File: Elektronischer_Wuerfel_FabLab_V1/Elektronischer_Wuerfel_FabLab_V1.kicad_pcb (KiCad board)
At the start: 2 copper layers, 20.9 x 20.9 mm, 21 parts, among them J1 Conn_01x02_Socket, J2 Conn_01x01_Socket, J3 Conn_01x06_Socket, U1 ATtiny85-20S

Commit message: some minor changes, repair of not connected A
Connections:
- U1 pad 6: unconnected-(U1-PB1-Pad6) -> /A
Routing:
- net /A: track 31.0 -> 35.4 mm, vias 0 -> 1
- net GND: track 4.86 -> 6.45 mm
- net VCC: track 10.5 -> 11.2 mm
- net /C: track 29.3 -> 29.9 mm
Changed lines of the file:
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@@
 	(net 14 "Net-(D6-A)")
 	(net 15 "Net-(D7-A)")
-	(net 16 "unconnected-(U1-PB1-Pad6)")
 	(footprint "Connector_PinHeader_2.00mm:PinHeader_1x02_P2.00mm_Vertical"
 		(layer "F.Cu")
@@
 			(size 1.7 0.65)
 			(layers "B.Cu" "B.Paste" "B.Mask")
-			(net 16 "unconnected-(U1-PB1-Pad6)")
+			(net 7 "/A")
 			(pinfunction "PB1")
 			(pintype "bidirectional")
@@
 	)
 	(segment
-		(start 176.036 73.1376)
-		(end 175.26 73.914)
+		(start 175.6075 73.5)
+		(end 176.036 73.0715)
 		(width 0.15)
 		(layer "F.Cu")
@@
 	)
 	(segment
-		(start 176.036 73.0715)
-		(end 176.036 73.1376)
+		(start 174.5 73.5)
+		(end 175.6075 73.5)
 		(width 0.15)
 		(layer "F.Cu")
@@
 	)
 	(via
-		(at 175.26 73.914)
+		(at 174.5 73.5)
 		(size 0.5)
 		(drill 0.4)
@@
 	)
 	(via
-		(at 175.26 75.184)
+		(at 175.26 75.5)
 		(size 0.5)
 		(drill 0.4)
@@
 	)
 	(segment
-		(start 175.26 73.914)
-		(end 175.26 75.184)
+		(start 174.5 73.5)
+		(end 175.26 74.26)
 		(width 0.15)
 		(layer "B.Cu")
@@
 	)
 	(segment
-		(start 172.211 70.4424)
-		(end 172.464 70.6947)
+		(start 175.26 74.26)
+		(end 175.26 75.5)
 		(width 0.15)
-		(layer "F.Cu")
-		(net 2)
+		(layer "B.Cu")
+		(net 1)
 	)
 	(segment
@@
 	)
 	(segment
-		(start 175.254 68.5073)
-		(end 174.993 68.7681)
+		(start 165.4092 71.2979)
+		(end 164.513 71.2979)
 		(width 0.15)
 		(layer "F.Cu")
@@
 	)
 	(segment
-		(start 172.464 71.0248)
-		(end 172.4635 71.0253)
+		(start 173.5 71)
+		(end 172.4888 71)
 		(width 0.15)
 		(layer "F.Cu")
@@
 	)
 	(segment
-		(start 177.333 73.7876)
-		(end 178.458 73.7876)
+		(start 172.464 71.0248)
+		(end 172.4635 71.0253)
 		(width 0.15)
 		(layer "F.Cu")
@@
 	)
 	(segment
-		(start 163.6 71.3887)
-		(end 164.422 71.3887)
+		(start 177.333 74)
+		(end 178.2455 74)
 		(width 0.15)
 		(layer "F.Cu")
@@
 	)
 	(segment
-		(start 175.76 68.5073)
-		(end 175.254 68.5073)
+		(start 178.2455 74)
+		(end 178.482 73.7635)
 		(width 0.15)
 		(layer "F.Cu")
@@
 	)
 	(segment
-		(start 178.458 73.7876)
-		(end 178.482 73.7635)
+		(start 178.23 66.548)
+		(end 178.412 66.548)
 		(width 0.15)
 		(layer "F.Cu")
@@
 	)
 	(segment
-		(start 164.422 71.3887)
-		(end 164.513 71.2979)
+		(start 172.4635 71.0253)
+		(end 172.4635 71.3549)
 		(width 0.15)
 		(layer "F.Cu")
@@
 	)
 	(segment
-		(start 178.23 66.548)
-		(end 178.412 66.548)
+		(start 172.4888 71)
+		(end 172.464 71.0248)
 		(width 0.15)
 		(layer "F.Cu")
@@
 	)
 	(segment
-		(start 172.4635 71.0253)
-		(end 172.4635 71.3549)
+		(start 163.686 67.9456)
+		(end 163.045 67.9456)
 		(width 0.15)
 		(layer "F.Cu")
@@
 	)
 	(segment
-		(start 163.686 67.9456)
-		(end 163.045 67.9456)
+		(start 175.7681 68.7681)
+		(end 174.993 68.7681)
 		(width 0.15)
 		(layer "F.Cu")
@@
 	)
 	(segment
-		(start 172.464 70.6947)
-		(end 172.464 71.0248)
+		(start 165.5 71.3887)
+		(end 165.4092 71.2979)
+		(width 0.15)
+		(layer "F.Cu")
+		(net 2)
+	)
+	(segment
+		(start 176 69)
+		(end 175.7681 68.7681)
 		(width 0.15)
 		(layer "F.Cu")
@@
 	)
 	(via
-		(at 172.211 70.4424)
+		(at 173.5 71)
 		(size 0.5)
 		(drill 0.4)
@@
 	)
 	(via
-		(at 163.6 71.3887)
+		(at 165.5 71.3887)
 		(size 0.5)
 		(drill 0.4)
@@
 	)
 	(via
-		(at 175.76 68.5073)
+		(at 176 69)
 		(size 0.5)
 		(drill 0.4)
@@
 	)
 	(via
-		(at 177.333 73.7876)
+		(at 177.333 74)
 		(size 0.5)
 		(drill 0.4)
@@
 	)
 	(segment
-		(start 178.287 64.9425)
-		(end 179.07 64.1591)
-		(width 0.15)
-		(layer "F.Cu")
-		(net 5)
-	)
-	(segment
 		(start 179.07 64.1591)
 		(end 180.033 65.1221)
@@
 	)
 	(segment
+		(start 178.61455 64.61455)
+		(end 179.07 64.1591)
+		(width 0.15)
+		(layer "F.Cu")
+		(net 5)
+	)
+	(segment
 		(start 178.4855 63.4702)
 		(end 178.486 63.4702)
@@
 	)
 	(via
-		(at 178.287 64.9425)
+		(at 178.61455 64.61455)
 		(size 0.5)
 		(drill 0.4)
@@
 	)
 	(segment
-		(start 170.1485 67.5828)
-		(end 170.148 67.5828)
+		(start 178.61455 64.61455)
+		(end 178.61455 64.61495)
 		(width 0.15)
 		(layer "B.Cu")
@@
 	)
 	(segment
-		(start 170.148 68.6595)
+		(start 174.57 68.6595)
+		(end 170.148 68.6595)
+		(width 0.15)
+		(layer "B.Cu")
+		(net 5)
+	)
+	(segment
+		(start 178.61455 64.61495)
 		(end 174.57 68.6595)
 		(width 0.15)
@@
 	)
 	(segment
-		(start 174.57 68.6595)
-		(end 178.287 64.9425)
+		(start 170.148 68.6595)
+		(end 170.148 67.5828)
 		(width 0.15)
 		(layer "B.Cu")
@@
 	(segment
 		(start 170.148 67.5828)
-		(end 170.148 68.6595)
+		(end 170.1485 67.5828)
 		(width 0.15)
 		(layer "B.Cu")
@@
 	)
 	(segment
+		(start 177.473429 73.475)
+		(end 178.479 72.469429)
+		(width 0.15)
+		(layer "F.Cu")
+		(net 6)
+	)
+	(segment
 		(start 171.099 70.7406)
 		(end 171.506 71.1469)
@@
 	)
 	(segment
+		(start 174.144 74.5569)
+		(end 176.391529 74.5569)
+		(width 0.15)
+		(layer "F.Cu")
+		(net 6)
+	)
+	(segment
 		(start 167.422 70.7406)
 		(end 171.099 70.7406)
@@
 	)
 	(segment
+		(start 176.391529 74.5569)
+		(end 176.808 74.140429)
+		(width 0.15)
+		(layer "F.Cu")
+		(net 6)
+	)
+	(segment
 		(start 162.462 71.5394)
 		(end 162.4622 71.5396)
@@
 	)
 	(segment
+		(start 176.808 73.782537)
+		(end 177.115537 73.475)
+		(width 0.15)
+		(layer "F.Cu")
+		(net 6)
+	)
+	(segment
 		(start 162.4624 71.5394)
 		(end 162.4622 71.5396)
@@
 	)
 	(segment
-		(start 175.84 74.5569)
-		(end 178.479 71.9178)
+		(start 178.479 72.469429)
+		(end 178.479 71.7286)
 		(width 0.15)
 		(layer "F.Cu")
@@
 	)
 	(segment
-		(start 171.506 71.1469)
-		(end 171.506 71.9179)
+		(start 176.808 74.140429)
+		(end 176.808 73.782537)
 		(width 0.15)
 		(layer "F.Cu")
@@
 	)
 	(segment
-		(start 178.479 71.9178)
-		(end 178.479 71.7286)
+		(start 171.506 71.1469)
+		(end 171.506 71.9179)
 		(width 0.15)
 		(layer "F.Cu")
@@
 	)
 	(segment
-		(start 174.144 74.5569)
-		(end 175.84 74.5569)
+		(start 177.115537 73.475)
+		(end 177.473429 73.475)
 		(width 0.15)
 		(layer "F.Cu")
@@
 	)
 	(segment
+		(start 170.5 76.5)
+		(end 171 76.5)
+		(width 0.15)
+		(layer "F.Cu")
+		(net 7)
+	)
+	(segment
 		(start 170.498 79.5307)
 		(end 169.926 78.9587)
@@
 	)
 	(segment
+		(start 169.926 77.074)
+		(end 170.5 76.5)
+		(width 0.15)
+		(layer "F.Cu")
+		(net 7)
+	)
+	(segment
 		(start 169.926 78.232)
 		(end 169.926 78.9587)
@@
 	)
 	(segment
+		(start 169.926 78.232)
+		(end 169.926 77.074)
+		(width 0.15)
+		(layer "F.Cu")
+		(net 7)
+	)
+	(segment
 		(start 161.533 74.1388)
 		(end 162.092 74.6977)
@@
 		(net 7)
 	)
+	(via
+		(at 171 76.5)
+		(size 0.5)
+		(drill 0.4)
+		(layers "F.Cu" "B.Cu")
+		(net 7)
+	)
+	(segment
+		(start 171 76.5)
+		(end 171.19773 76.5)
+		(width 0.15)
+		(layer "B.Cu")
+		(net 7)
+	)
+	(segment
+		(start 171.19773 76.5)
+		(end 171.4185 76.27923)
+		(width 0.15)
+		(layer "B.Cu")
+		(net 7)
+	)
+	(segment
+		(start 171.4185 76.27923)
+		(end 171.4185 74.8828)
+		(width 0.15)
+		(layer "B.Cu")
+		(net 7)
+	)

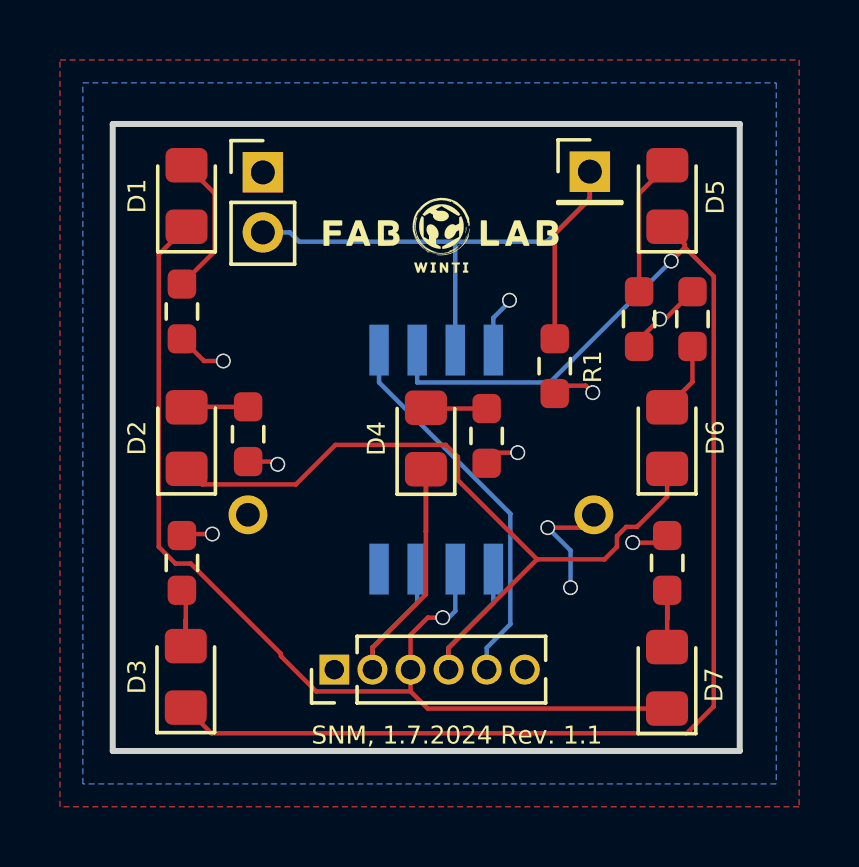
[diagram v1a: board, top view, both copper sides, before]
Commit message: Moved tilt switch a bit to give more space at the board edge.
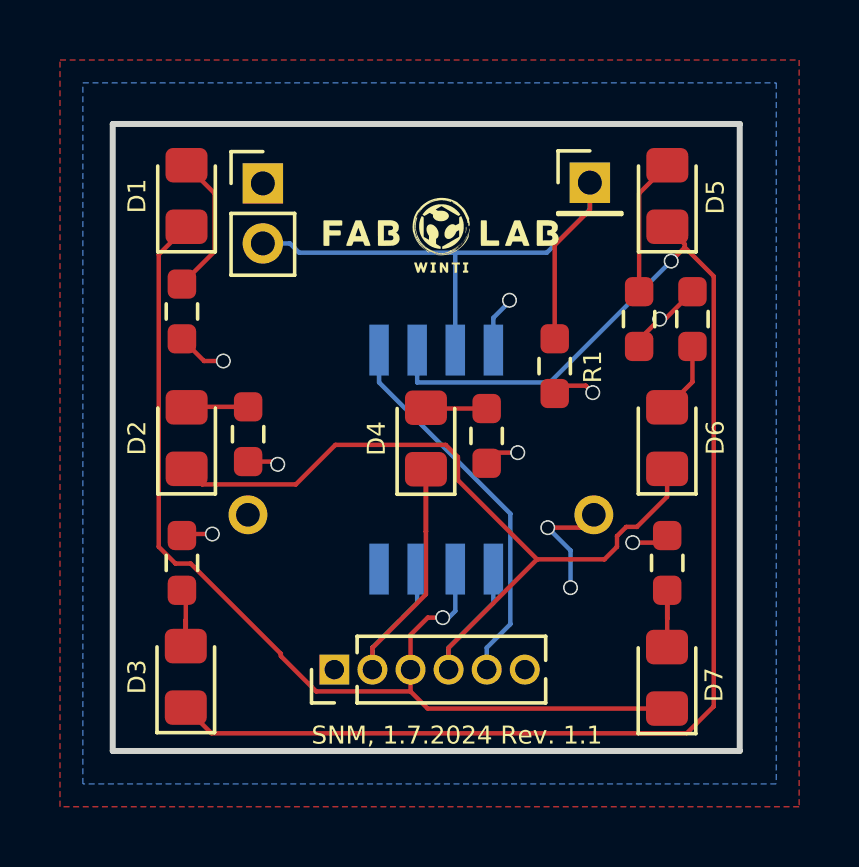
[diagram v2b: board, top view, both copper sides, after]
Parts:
- moved J1 0.37 mm to (165.0, 62.0)
- moved J2 0.37 mm to (175.9, 62.0)
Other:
- board text added: "Tilt-Switch"
- board text removed: "Tilt Switch"
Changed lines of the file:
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@@
 	(footprint "Connector_PinHeader_2.00mm:PinHeader_1x02_P2.00mm_Vertical"
 		(layer "F.Cu")
-		(at 165.0038 61.659)
+		(at 165.0038 62.0258)
 		(descr "Through hole straight pin header, 1x02, 2.00mm pitch, single row")
 		(tags "Through hole pin header THT 1x02 2.00mm single row")
@@
 	(footprint "Connector_PinHeader_2.00mm:PinHeader_1x01_P2.00mm_Vertical"
 		(layer "F.Cu")
-		(at 175.9037 61.6332)
+		(at 175.9037 62)
 		(descr "Through hole straight pin header, 1x01, 2.00mm pitch, single row")
 		(tags "Through hole pin header THT 1x01 2.00mm single row")
@@
 	)
 	(gr_line
-		(start 175.85798 63.097182)
-		(end 175.85798 62.589182)
+		(start 175.85798 63.984)
+		(end 175.85798 63.476)
 		(stroke
 			(width 0.15)
@@
 	)
 	(gr_line
-		(start 175.85798 64.113182)
-		(end 175.85798 63.097182)
+		(start 175.85798 64.5)
+		(end 175.85798 63.984)
 		(stroke
 			(width 0.15)
@@
 	)
 	(gr_line
-		(start 166.37 64.113182)
-		(end 175.85798 64.113182)
+		(start 166.37 64.5)
+		(end 175.85798 64.5)
 		(stroke
 			(width 0.15)
@@
 	)
 	(gr_text "T"
-		(at 177.168883 61.91478 0)
+		(at 177.54325 62.206113 0)
 		(layer "B.SilkS")
 		(effects
@@
 	)
 	(gr_text "GND"
-		(at 165.824004 60.893508 0)
+		(at 163.734738 62.330795 0)
 		(layer "B.SilkS")
 		(effects
@@
 	)
 	(gr_text "T"
-		(at 164.095966 63.970004 0)
+		(at 163.952931 64.325704 0)
 		(layer "B.SilkS")
 		(effects
@@
 		)
 	)
-	(gr_text "Tilt Switch"
+	(gr_text "Tilt-Switch"
 		(at 174.498 62.738 0)
 		(layer "B.SilkS")
@@
 	)
 	(segment
-		(start 174.7324 67.2039)
-		(end 174.732 67.2039)
+		(start 175.904 62.906994)
+		(end 174.732 64.078994)
 		(width 0.15)
 		(layer "F.Cu")
@@
 	)
 	(segment
-		(start 174.732 63.7062)
-		(end 174.732 67.2039)
+		(start 175.9037 61.6332)
+		(end 175.904 61.6332)
 		(width 0.15)
 		(layer "F.Cu")
@@
 	)
 	(segment
-		(start 175.9037 61.6332)
-		(end 175.904 61.6332)
+		(start 175.904 61.6332)
+		(end 175.904 62.906994)
 		(width 0.15)
 		(layer "F.Cu")
@@
 	)
 	(segment
-		(start 175.904 62.5349)
-		(end 174.732 63.7062)
+		(start 174.732 64.078994)
+		(end 174.732 67.2039)
 		(width 0.15)
 		(layer "F.Cu")
@@
 	)
 	(segment
-		(start 175.904 61.6332)
-		(end 175.904 62.5349)
+		(start 174.732 67.2039)
+		(end 174.7324 67.2039)
 		(width 0.15)
 		(layer "F.Cu")
@@
 	)
 	(segment
-		(start 166.214 63.968)
-		(end 165.906 63.659)
+		(start 166.214 64.3348)
+		(end 165.906 64.0258)
 		(width 0.15)
 		(layer "B.Cu")
@@
 	)
 	(segment
-		(start 171.418 63.968)
-		(end 166.214 63.968)
+		(start 171.418 64.3348)
+		(end 166.214 64.3348)
 		(width 0.15)
 		(layer "B.Cu")
@@
 	)
 	(segment
-		(start 175.904 62.5349)
-		(end 174.471 63.968)
+		(start 175.904 62.9017)
+		(end 174.471 64.3348)
 		(width 0.15)
 		(layer "B.Cu")
@@
 	)
 	(segment
-		(start 174.471 63.968)
-		(end 171.418 63.968)
+		(start 174.471 64.3348)
+		(end 171.418 64.3348)
 		(width 0.15)
 		(layer "B.Cu")
@@
 	)
 	(segment
-		(start 165.906 63.659)
-		(end 165.004 63.659)
+		(start 165.906 64.0258)
+		(end 165.004 64.0258)
 		(width 0.15)
 		(layer "B.Cu")
@@
 	)
 	(segment
-		(start 175.9037 62.0837)
-		(end 175.9037 61.6332)
+		(start 175.9037 62.4505)
+		(end 175.9037 62)
 		(width 0.15)
 		(layer "B.Cu")
@@
 	)
 	(segment
-		(start 175.904 61.6332)
-		(end 175.904 62.084)
+		(start 175.904 62)
+		(end 175.904 62.4508)
 		(width 0.15)
 		(layer "B.Cu")
@@
 	)
 	(segment
-		(start 171.418 67.5828)
-		(end 171.418 63.968)
+		(start 171.418 67.9496)
+		(end 171.418 64.3348)
 		(width 0.15)
 		(layer "B.Cu")
@@
 	)
 	(segment
-		(start 175.904 62.084)
-		(end 175.904 62.5349)
+		(start 175.904 62.4508)
+		(end 175.904 62.9017)
 		(width 0.15)
 		(layer "B.Cu")
